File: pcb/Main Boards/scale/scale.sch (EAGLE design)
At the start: 26 parts, among them IC1 DS18B20+, J3 Spring Terminal, U1 NAU7802, X1 RJ45-8X

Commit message: Minor changes and cleanup
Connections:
- net A+: now also J3.3
- net A-: now also J3.4
- net GND: now also J3.2
- net VDDA: now also J3.1
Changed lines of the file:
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@@
 <wire x1="-45.72" y1="-10.16" x2="-45.72" y2="-17.78" width="0.1524" layer="91"/>
 <pinref part="GND1" gate="1" pin="GND"/>
+<pinref part="J3" gate="J1" pin="2"/>
+<wire x1="-58.42" y1="-10.16" x2="-45.72" y2="-10.16" width="0.1524" layer="91"/>
 </segment>
 </net>
@@
 <wire x1="-45.72" y1="-7.62" x2="-45.72" y2="-5.08" width="0.1524" layer="91"/>
 <pinref part="U$10" gate="G$1" pin="VDDA"/>
+<pinref part="J3" gate="J1" pin="1"/>
+<wire x1="-58.42" y1="-7.62" x2="-45.72" y2="-7.62" width="0.1524" layer="91"/>
 </segment>
 </net>
@@
 <label x="43.18" y="35.56" size="1.27" layer="95" rot="R180" xref="yes"/>
 </segment>
+<segment>
+<pinref part="J3" gate="J1" pin="4"/>
+<wire x1="-58.42" y1="-15.24" x2="-50.8" y2="-15.24" width="0.1524" layer="91"/>
+<label x="-53.34" y="-15.24" size="1.778" layer="95"/>
+</segment>
 </net>
 <net name="A+" class="0">
@@
 <label x="43.18" y="22.86" size="1.27" layer="95" rot="R180" xref="yes"/>
 </segment>
-</net>
+<segment>
+<pinref part="J3" gate="J1" pin="3"/>
+<wire x1="-58.42" y1="-12.7" x2="-50.8" y2="-12.7" width="0.1524" layer="91"/>
+<label x="-53.34" y="-12.7" size="1.778" layer="95"/>
+</segment>
+</net>

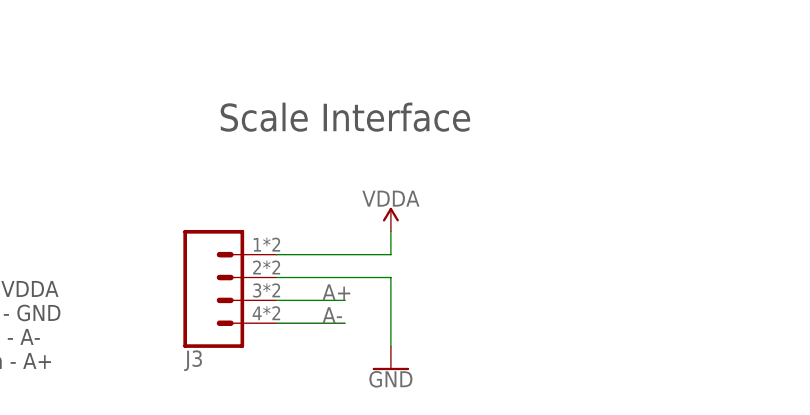
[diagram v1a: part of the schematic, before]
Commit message: Add scale terminal
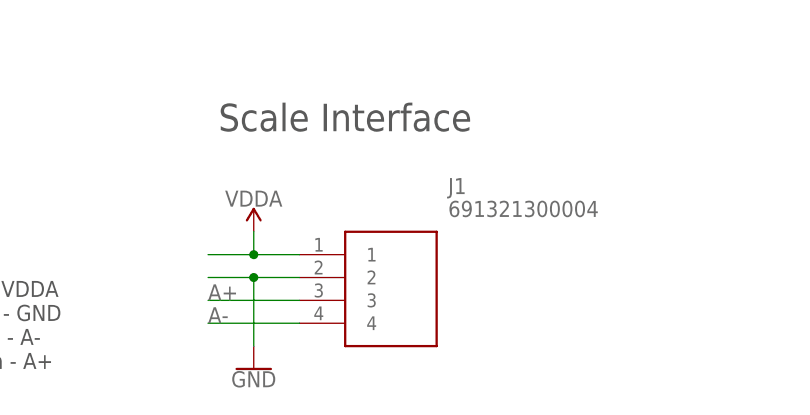
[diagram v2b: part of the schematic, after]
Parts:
- removed J3: Spring Terminal, SparkFun-Connectors:CONN_04SPRING
- added J1: 691321300004, SamacSys_Parts:691321300004
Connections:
- net A+: now also J1.3; no longer J3.3
- net A-: now also J1.4; no longer J3.4
- net GND: now also J1.2; no longer J3.2
- net VDDA: now also J1.1; no longer J3.1
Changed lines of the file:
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@@
 <part name="R8" library="SparkFun-Resistors" library_urn="urn:adsk.eagle:library:532" deviceset="1KOHM" device="-HORIZ-1/4W-5%" package3d_urn="urn:adsk.eagle:package:39658/1" value="2.2kΩ"/>
 <part name="R9" library="SparkFun-Resistors" library_urn="urn:adsk.eagle:library:532" deviceset="1KOHM" device="-HORIZ-1/4W-5%" package3d_urn="urn:adsk.eagle:package:39658/1" value="2.2kΩ"/>
-<part name="J3" library="SparkFun-Connectors" deviceset="CONN_04" device="SPRING" value="Spring Terminal"/>
 <part name="C5" library="Donnie" deviceset="CAP_CERAMIC_2.54" device="" value="0.1μF"/>
 <part name="C6" library="Donnie" deviceset="CAP_CERAMIC_2.54" device="" value="0.1μF"/>
@@
 <part name="C9" library="Donnie" deviceset="CAP_CERAMIC_2.54" device="" value="330pF"/>
 <part name="C7" library="Donnie" deviceset="CAP_CERAMIC_2.54" device="" value="0.1μF"/>
+<part name="J1" library="SamacSys_Parts" deviceset="691321300004" device=""/>
 </parts>
 <sheets>
@@
 <attribute name="VALUE" x="51.562" y="24.638" size="1.778" layer="96" font="vector"/>
 </instance>
-<instance part="GND1" gate="1" x="-45.72" y="-20.32" smashed="yes">
-<attribute name="VALUE" x="-45.72" y="-20.574" size="1.778" layer="96" font="vector" align="top-center"/>
-</instance>
-<instance part="U$10" gate="G$1" x="-45.72" y="-5.08" smashed="yes">
-<attribute name="VALUE" x="-45.72" y="-2.286" size="1.778" layer="96" font="vector" align="bottom-center"/>
+<instance part="GND1" gate="1" x="-60.96" y="-20.32" smashed="yes">
+<attribute name="VALUE" x="-60.96" y="-20.574" size="1.778" layer="96" font="vector" align="top-center"/>
+</instance>
+<instance part="U$10" gate="G$1" x="-60.96" y="-5.08" smashed="yes">
+<attribute name="VALUE" x="-60.96" y="-2.286" size="1.778" layer="96" font="vector" align="bottom-center"/>
 </instance>
 <instance part="SUPPLY1" gate="G$1" x="124.46" y="45.72" smashed="yes"/>
@@
 <attribute name="VALUE" x="133.604" y="30.48" size="1.778" layer="96" font="vector" rot="R90" align="top-center"/>
 </instance>
-<instance part="J3" gate="J1" x="-63.5" y="-10.16" smashed="yes" rot="MR180">
-<attribute name="NAME" x="-68.58" y="-18.288" size="1.778" layer="95" font="vector" rot="MR180"/>
-</instance>
 <instance part="C5" gate="G$1" x="58.42" y="25.4" smashed="yes">
 <attribute name="NAME" x="59.944" y="30.861" size="1.778" layer="95" font="vector"/>
@@
 <attribute name="NAME" x="67.056" y="7.239" size="1.778" layer="95" font="vector" rot="R180"/>
 <attribute name="VALUE" x="67.056" y="12.319" size="1.778" layer="96" font="vector" rot="R180"/>
+</instance>
+<instance part="J1" gate="G$1" x="-55.88" y="-7.62" smashed="yes">
+<attribute name="NAME" x="-39.37" y="0" size="1.778" layer="95" align="center-left"/>
+<attribute name="VALUE" x="-39.37" y="-2.54" size="1.778" layer="96" align="center-left"/>
 </instance>
 </instances>
@@
 </segment>
 <segment>
-<wire x1="-45.72" y1="-10.16" x2="-45.72" y2="-17.78" width="0.1524" layer="91"/>
+<wire x1="-60.96" y1="-10.16" x2="-60.96" y2="-17.78" width="0.1524" layer="91"/>
 <pinref part="GND1" gate="1" pin="GND"/>
-<pinref part="J3" gate="J1" pin="2"/>
-<wire x1="-58.42" y1="-10.16" x2="-45.72" y2="-10.16" width="0.1524" layer="91"/>
+<wire x1="-66.04" y1="-10.16" x2="-60.96" y2="-10.16" width="0.1524" layer="91"/>
+<pinref part="J1" gate="G$1" pin="2"/>
+<wire x1="-60.96" y1="-10.16" x2="-55.88" y2="-10.16" width="0.1524" layer="91"/>
+<junction x="-60.96" y="-10.16"/>
 </segment>
 </net>
@@
 </segment>
 <segment>
-<wire x1="-45.72" y1="-7.62" x2="-45.72" y2="-5.08" width="0.1524" layer="91"/>
+<wire x1="-60.96" y1="-7.62" x2="-60.96" y2="-5.08" width="0.1524" layer="91"/>
 <pinref part="U$10" gate="G$1" pin="VDDA"/>
-<pinref part="J3" gate="J1" pin="1"/>
-<wire x1="-58.42" y1="-7.62" x2="-45.72" y2="-7.62" width="0.1524" layer="91"/>
+<wire x1="-66.04" y1="-7.62" x2="-60.96" y2="-7.62" width="0.1524" layer="91"/>
+<pinref part="J1" gate="G$1" pin="1"/>
+<wire x1="-60.96" y1="-7.62" x2="-55.88" y2="-7.62" width="0.1524" layer="91"/>
+<junction x="-60.96" y="-7.62"/>
 </segment>
 </net>
@@
 </segment>
 <segment>
-<pinref part="J3" gate="J1" pin="4"/>
-<wire x1="-58.42" y1="-15.24" x2="-50.8" y2="-15.24" width="0.1524" layer="91"/>
-<label x="-53.34" y="-15.24" size="1.778" layer="95"/>
+<label x="-66.04" y="-15.24" size="1.778" layer="95"/>
+<pinref part="J1" gate="G$1" pin="4"/>
+<wire x1="-66.04" y1="-15.24" x2="-55.88" y2="-15.24" width="0.1524" layer="91"/>
 </segment>
 </net>
@@
 </segment>
 <segment>
-<pinref part="J3" gate="J1" pin="3"/>
-<wire x1="-58.42" y1="-12.7" x2="-50.8" y2="-12.7" width="0.1524" layer="91"/>
-<label x="-53.34" y="-12.7" size="1.778" layer="95"/>
-</segment>
-</net>
+<label x="-66.04" y="-12.7" size="1.778" layer="95"/>
+<pinref part="J1" gate="G$1" pin="3"/>
+<wire x1="-66.04" y1="-12.7" x2="-55.88" y2="-12.7" width="0.1524" layer="91"/>
+</segment>
+</net>
